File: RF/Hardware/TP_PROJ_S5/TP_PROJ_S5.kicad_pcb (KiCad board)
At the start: 2 copper layers, 30 parts, among them J1 Connecteur STLINK V3, J2 DIN-5, J3 Batterie, U1 STM32WB55CEUx, U2 BU33SD5WG-TR, U3 DLF162500LT-5028A1

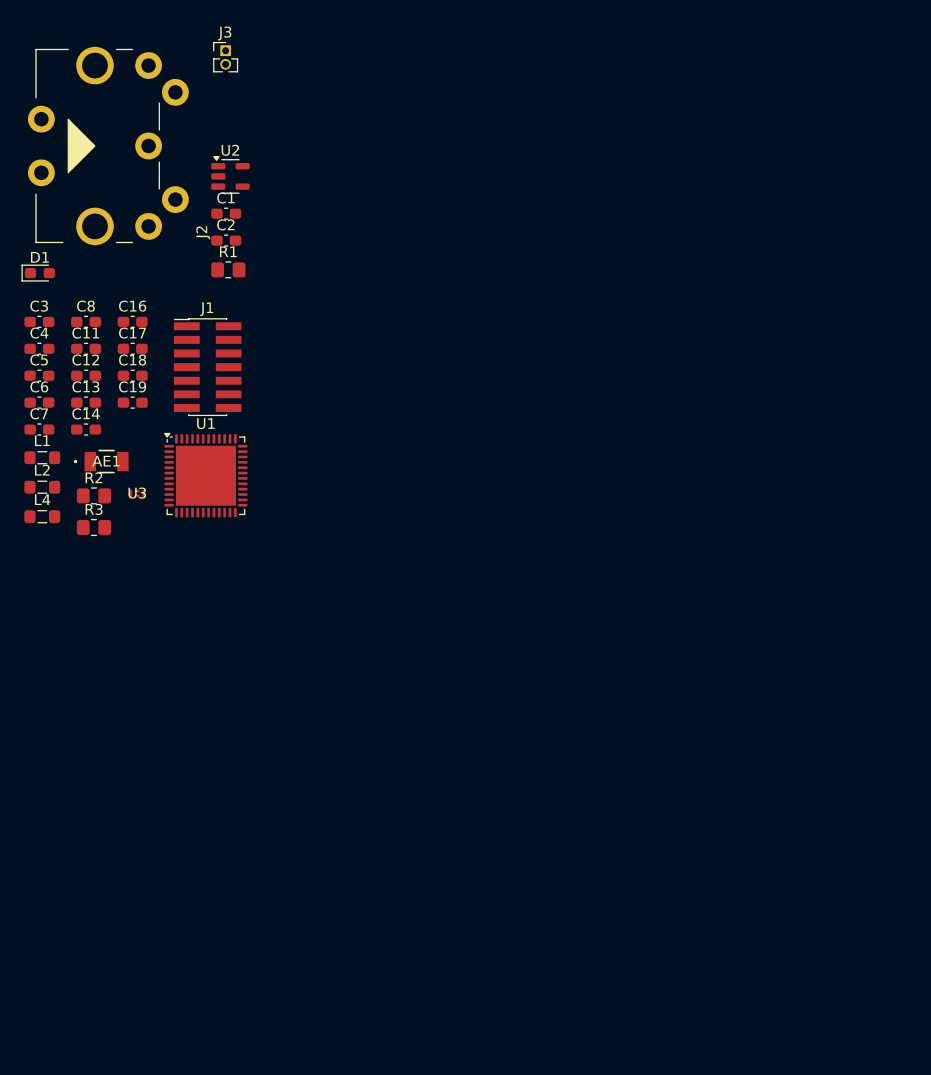
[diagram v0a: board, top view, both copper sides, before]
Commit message: Ajout schéma routage et fichiers gerber
Création et finalisation de schémas routage, électrique et ajouts fichiers gerber
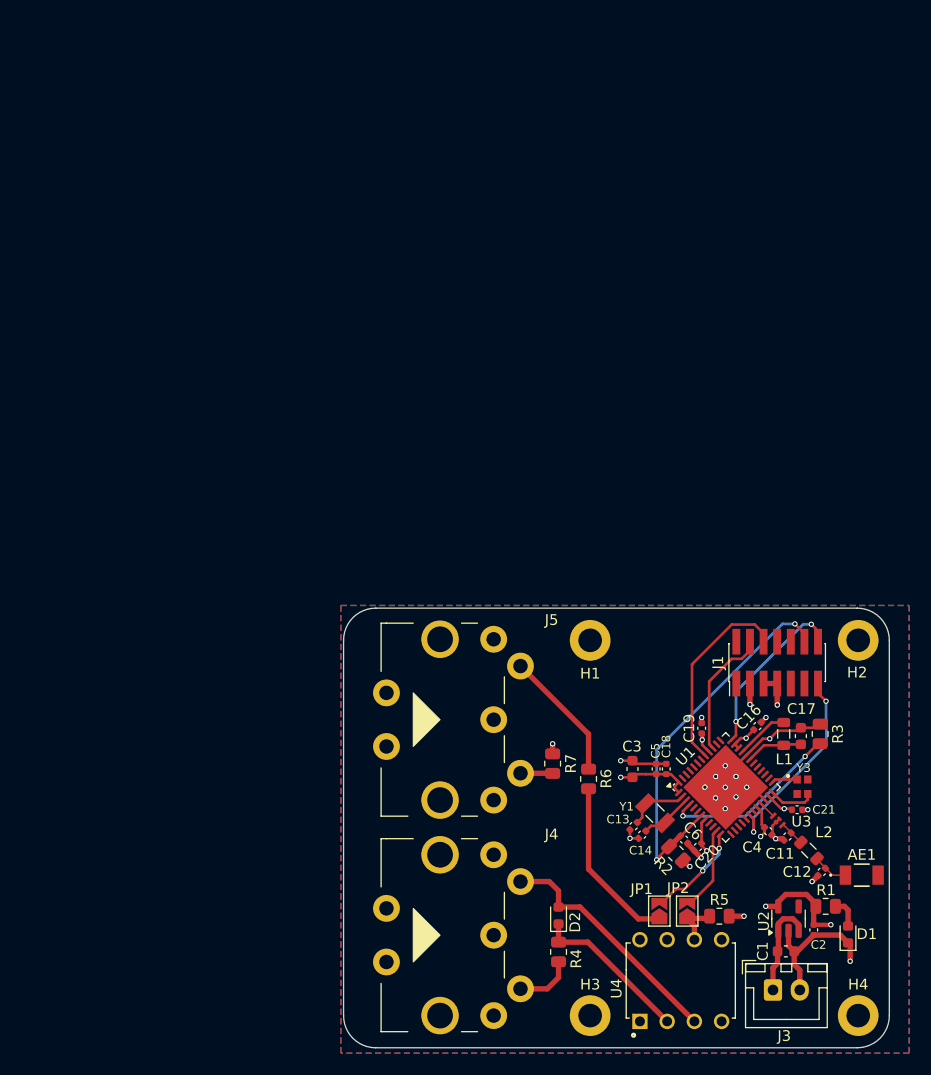
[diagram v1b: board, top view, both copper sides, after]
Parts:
- removed C7: 1u, Capacitor_SMD:C_0603_1608Metric_Pad1.08x0.95mm_HandSolder
- removed C8: 10n, Capacitor_SMD:C_0603_1608Metric_Pad1.08x0.95mm_HandSolder
- removed J2: DIN-5, footprints:DIN5_MIDI
- removed L4: 39nH, Inductor_SMD:L_0805_2012Metric_Pad1.05x1.20mm_HandSolder
- added C20: 100n, Capacitor_SMD:C_0402_1005Metric, F.Cu at (134.1, 119.3)
- added C21: 100n, Capacitor_SMD:C_0402_1005Metric, F.Cu at (143.3, 115.8)
- added D2: D, LED_SMD:LED_0603_1608Metric, F.Cu at (121.0, 125.7)
- added H1: MountingHole_Pad, MountingHole:MountingHole_2.2mm_M2_DIN965_Pad, F.Cu at (124.0, 100.0)
- added H2: MountingHole_Pad, MountingHole:MountingHole_2.2mm_M2_DIN965_Pad, F.Cu at (149.0, 100.0)
- added H3: MountingHole_Pad, MountingHole:MountingHole_2.2mm_M2_DIN965_Pad, F.Cu at (124.0, 135.0)
- added H4: MountingHole_Pad, MountingHole:MountingHole_2.2mm_M2_DIN965_Pad, F.Cu at (149.0, 135.0)
- added J4: DIN-5, footprints:DIN5_MIDI, F.Cu at (115.0, 127.5)
- added J5: DIN-5, footprints:DIN5_MIDI, F.Cu at (115.0, 107.4)
- added JP1: SolderJumper_2_Open, Jumper:SolderJumper-2_P1.3mm_Open_TrianglePad1.0x1.5mm, F.Cu at (130.4, 125.3)
- added JP2: SolderJumper_2_Open, Jumper:SolderJumper-2_P1.3mm_Open_TrianglePad1.0x1.5mm, F.Cu at (133.1, 125.3)
- added R4: 220, Resistor_SMD:R_0805_2012Metric, F.Cu at (121.0, 129.1)
- added R5: 270, Resistor_SMD:R_0805_2012Metric, F.Cu at (136.1, 125.7)
- added R6: 220, Resistor_SMD:R_0805_2012Metric, F.Cu at (123.8, 112.9)
- added R7: 220, Resistor_SMD:R_0805_2012Metric, F.Cu at (120.5, 111.5)
- added U4: 6N138, footprints:DIP762W50P254L1018H450Q8, F.Cu at (132.4, 131.7)
- added Y1: 32k, footprints:XTAL_ABS07AIG32.768KHZ6DT, F.Cu at (130.1, 116.1)
- added Y3: 32M, footprints:OSC_XRCGB32M000F2P01R0, F.Cu at (143.8, 113.7)
- C1, C17, C3: footprint Capacitor_SMD:C_0603_1608Metric_Pad1.08x0.95mm_HandSolder -> Capacitor_SMD:C_0603_1608Metric
- C11, C12: value C -> 1.2pF; footprint Capacitor_SMD:C_0603_1608Metric_Pad1.08x0.95mm_HandSolder -> Capacitor_SMD:C_0402_1005Metric
- C13, C14: value C -> 8pF; footprint Capacitor_SMD:C_0603_1608Metric_Pad1.08x0.95mm_HandSolder -> Capacitor_SMD:C_0402_1005Metric
- C16, C18, C19, C2, C4, C5, C6: footprint Capacitor_SMD:C_0603_1608Metric_Pad1.08x0.95mm_HandSolder -> Capacitor_SMD:C_0402_1005Metric
- D1: footprint LED_SMD:LED_0603_1608Metric_Pad1.05x0.95mm_HandSolder -> LED_SMD:LED_0603_1608Metric
- J3: footprint Connector_PinHeader_1.27mm:PinHeader_1x02_P1.27mm_Vertical -> Connector_JST:JST_XH_B2B-XH-A_1x02_P2.50mm_Vertical
- L1: value 2,2 µF -> 2.2µF; footprint Inductor_SMD:L_0805_2012Metric_Pad1.05x1.20mm_HandSolder -> Inductor_SMD:L_0805_2012Metric
- L2: value L -> 3.6nH; footprint Inductor_SMD:L_0805_2012Metric_Pad1.05x1.20mm_HandSolder -> Inductor_SMD:L_0805_2012Metric
- R1, R2, R3: footprint Resistor_SMD:R_0805_2012Metric_Pad1.20x1.40mm_HandSolder -> Resistor_SMD:R_0805_2012Metric
- moved J3 101.4 mm to (141.1, 132.6)
- moved D1 97.4 mm to (148.1, 127.4), turned to 90 degrees
- moved U2 86.6 mm to (142.5, 126.0), turned to 90 degrees
- moved C1 86.4 mm to (142.2, 129.0)
- moved C2 84.5 mm to (144.8, 127.0), turned to -90 degrees
- moved C12 82.8 mm to (145.6, 121.6), turned to -135 degrees
- moved C4 81.5 mm to (140.6, 117.8), turned to -45 degrees
- moved R1 81.4 mm to (146.0, 124.8)
- moved AE1 80.3 mm to (149.3, 121.9)
- moved C11 79.7 mm to (142.4, 118.3), turned to -135 degrees
- moved L2 79.1 mm to (144.4, 119.6), turned to -45 degrees
- moved L1 73.8 mm to (142.1, 108.7), turned to 90 degrees
- moved C6 72.6 mm to (132.8, 118.6), turned to -45 degrees
- moved C17 72.0 mm to (143.7, 108.9), turned to 90 degrees
- moved R3 70.4 mm to (145.4, 108.7), turned to -90 degrees
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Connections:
- net Net-(J1-JCLK/SWCLK) renamed /stm32/JCLK/SWCLK
- net Net-(J1-JTMS/SWDIO) renamed /stm32/JTMS/SWDIO
- net Net-(J1-VCP_RX) renamed /stm32/VCP_RX
- net Net-(J1-VCP_TX) renamed /stm32/VCP_TX
- U1 pad 8: +3.3VA -> +3.3V
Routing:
- net GND: track 0.00 -> 46.7 mm, vias 0 -> 20
- net /stm32/NRST: track 0.00 -> 36.0 mm, vias 0 -> 2
- net +3.3V: track 0.00 -> 35.7 mm, vias 0 -> 12
- net Net-(D2-A): track 0.00 -> 22.5 mm
- net /stm32/VCP_RX: track 0.00 -> 18.7 mm, vias 0 -> 2
- net /stm32/JCLK/SWCLK: track 0.00 -> 18.4 mm
- net Net-(U1-PH3): track 0.00 -> 17.0 mm, vias 0 -> 2
- net /stm32/VCP_TX: track 0.00 -> 16.4 mm, vias 0 -> 2
- net Net-(JP1-A): track 0.00 -> 16.0 mm
- net Net-(D2-K): track 0.00 -> 14.9 mm
- net Net-(J5-Pad5): track 0.00 -> 12.3 mm
- net /stm32/JTMS/SWDIO: track 0.00 -> 12.2 mm
- net BATT: track 0.00 -> 9.48 mm
- net /stm32/TX_MIDI: track 0.00 -> 9.40 mm, vias 0 -> 2
- net /stm32/RX_MIDI: track 0.00 -> 8.11 mm
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- added copper zone on B.Cu, net (none)
- added copper zone on F.Cu, net (none)
- added copper zone on In2.Cu, net +3.3V
- added copper zone on In1.Cu, net GND
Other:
- board outline added: 50.9 x 41 mm
- copper layers 2 -> 4
- board text added: "G-Loiselet A-Taillepierre G-Vidon"
